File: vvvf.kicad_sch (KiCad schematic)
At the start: 106 parts, among them J1 Screw_Terminal_01x01, J2 Screw_Terminal_01x01, J3 Screw_Terminal_01x01, J4 Screw_Terminal_01x01, J5 Screw_Terminal_01x01, J6 Screw_Terminal_01x02, Q1 Q_NIGBT_GCE, Q2 Q_NIGBT_GCE, Q3 IPDD60R037CM8XTMA1, Q4 IPDD60R037CM8XTMA1, Q5 IPDD60R037CM8XTMA1, Q6 IPDD60R037CM8XTMA1, Q7 IPDD60R037CM8XTMA1, Q8 IPDD60R037CM8XTMA1, Q9 IPDD60R037CM8XTMA1, SW1 SW_Push, U1 TLP152, U2 TLP152, U3 UCC21520ADW, U4 TLP152, U5 ACS770xCB-200B-PFF, U6 UCC21520ADW, U7 UCC21520ADW, U8 ACS770xCB-200B-PFF

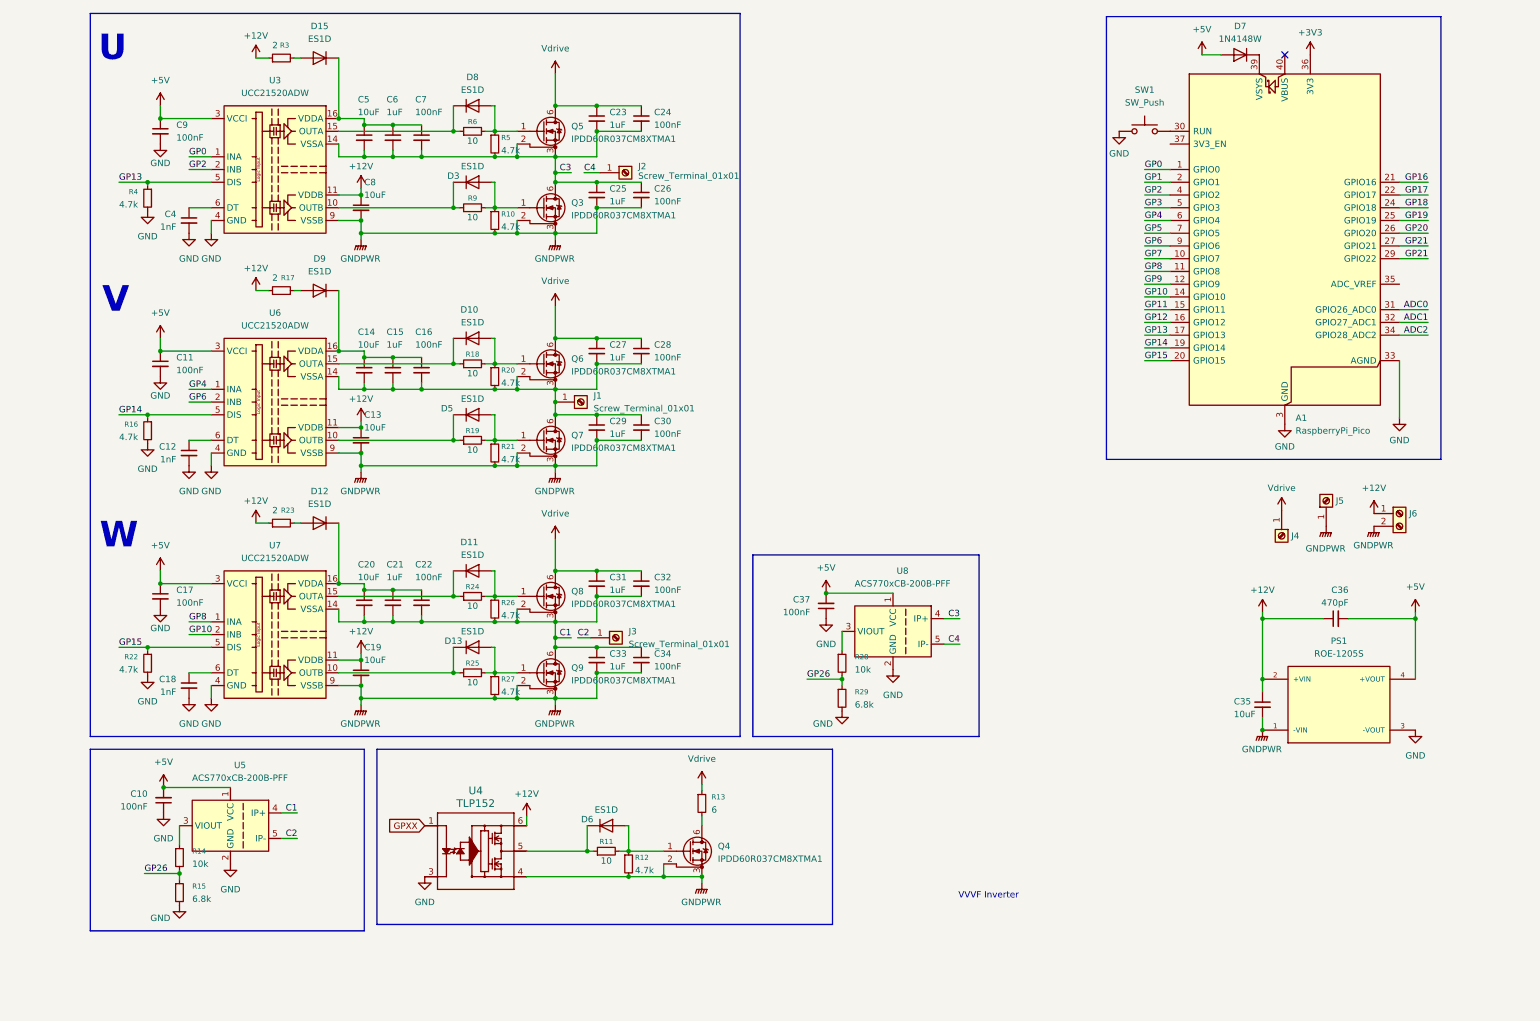
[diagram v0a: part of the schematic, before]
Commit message: Starting new routing with external IGBT
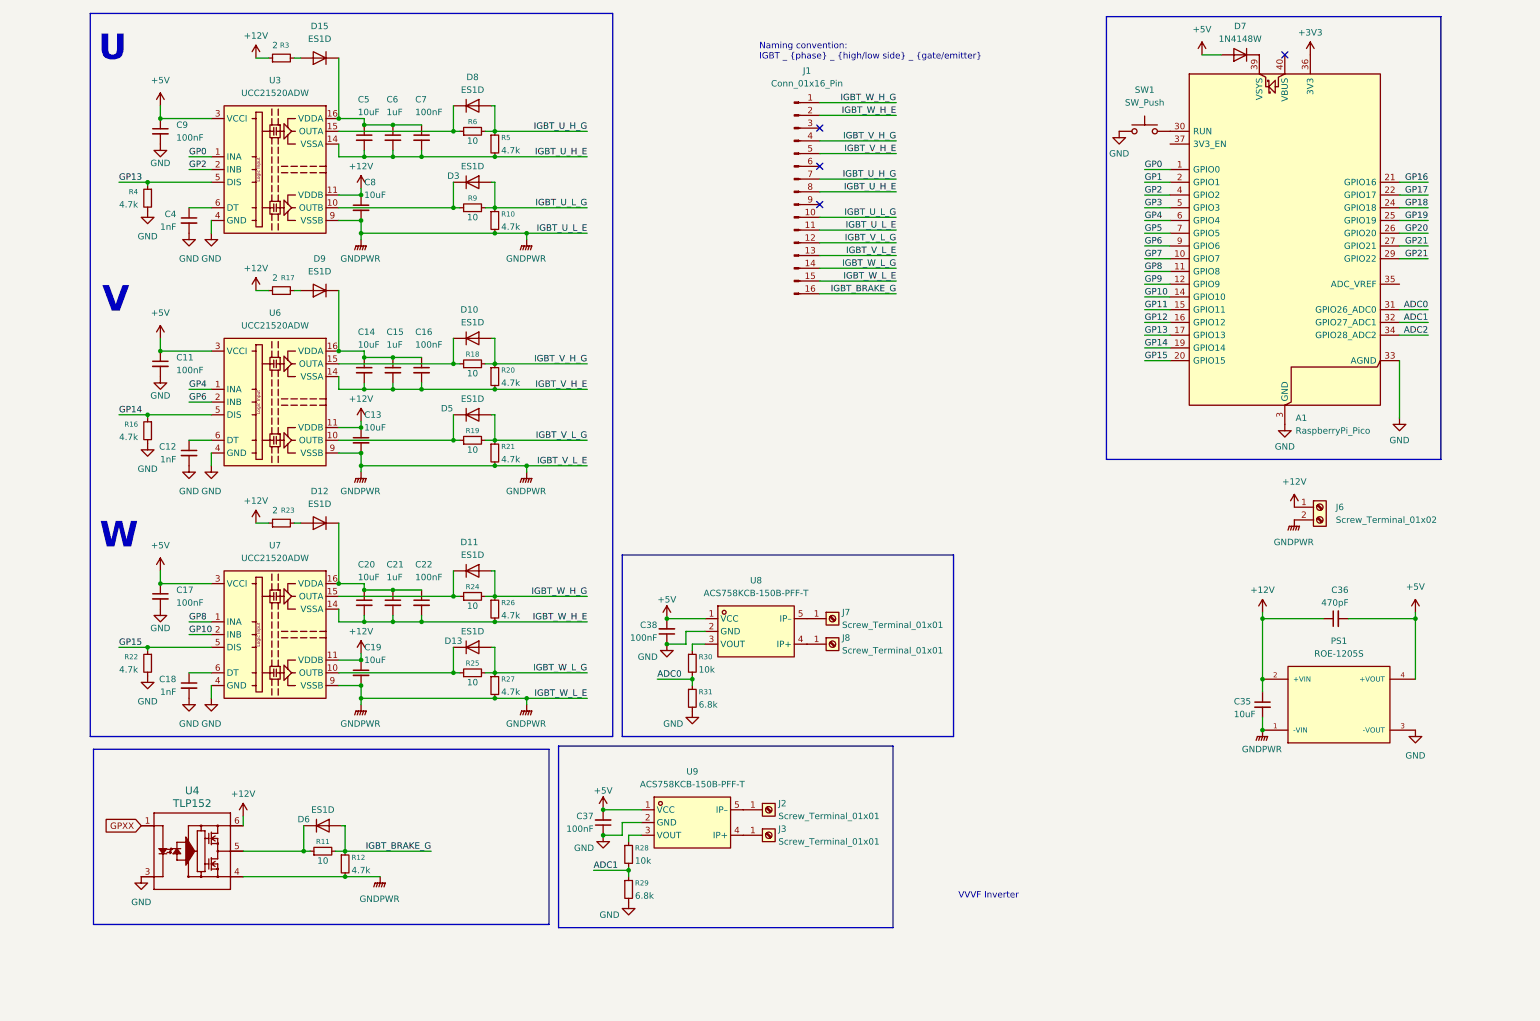
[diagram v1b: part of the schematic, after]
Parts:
- removed C10: 100nF, Capacitor_SMD:C_0603_1608Metric_Pad1.08x0.95mm_HandSolder, symbol Device:C_Small
- removed C23, C25, C27, C29, C31, C33: 1uF, Snapeda:B32923C3105M000_CAPRR2250W80L2650T1100H2050, symbol Device:C_Small
- removed C24, C26, C28, C30, C32, C34: 100nF, Snapeda:B32922C3104K289_CAPRR1500W80L1800T500H1050, symbol Device:C_Small
- removed J1, J4, J5: Screw_Terminal_01x01, symbol Connector:Screw_Terminal_01x01
- removed Q3, Q4, Q5, Q6, Q7, Q8, Q9: IPDD60R037CM8XTMA1, Package_TO_SOT_SMD:Infineon_PG-HDSOP-10-1, symbol Transistor_FET:IPDD60R050G7
- removed R13: 6, symbol Device:R_Small
- removed R14: 10k, Resistor_SMD:R_0603_1608Metric_Pad0.98x0.95mm_HandSolder, symbol Device:R_Small
- removed R15: 6.8k, symbol Device:R_Small
- removed U5, U8: ACS770xCB-200B-PFF, Sensor_Current:Allegro_CB_PFF, symbol Sensor_Current:ACS770xCB-200B-PFF
- added C38: 100nF, Capacitor_SMD:C_0603_1608Metric_Pad1.08x0.95mm_HandSolder, symbol Device:C_Small
- added J1: Conn_01x16_Pin, Connector_PinHeader_2.54mm:PinHeader_1x16_P2.54mm_Vertical, symbol Connector:Conn_01x16_Pin
- added J7, J8: Screw_Terminal_01x01, easyeda2kicad:CONN-TH_T44001, symbol Connector:Screw_Terminal_01x01
- added R30: 10k, Resistor_SMD:R_0603_1608Metric_Pad0.98x0.95mm_HandSolder, symbol Device:R_Small
- added R31: 6.8k, symbol Device:R_Small
- added U8, U9: ACS758KCB-150B-PFF-T, easyeda2kicad:SENSOR-TH_ACS758KCB-150B-PFF-T, symbol easyeda2kicad:ACS758KCB-150B-PFF-T_C6396159
- J2, J3: footprint (none) -> easyeda2kicad:CONN-TH_T44001
- J6: footprint (none) -> easyeda2kicad:CONN-TH_WJ126V-5.0-2P
- U3, U6, U7: LCSC Part (none) -> C2863027
- U4: footprint 5pin SO6_TOS -> Package_SO:SO-5-6_4.55x3.7mm_P1.27mm
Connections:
- net GP26 is gone; now on net ADC1: R28.2, R29.1
- net +5V: now also C38.2, U8.1 (VCC), U9.1 (VCC)
- net ADC0: now also R30.2, R31.1
- net GND: now also C38.1, R31.2, U8.2 (GND), U9.2 (GND)
- net GNDPWR: now also J1.11 (Pin_11), J1.13 (Pin_13), J1.15 (Pin_15)
- net IGBT_W_H_G: now reaches D11.2 (A), R24.2, R26.1
- net IGBT_W_H_G: now also J1.1 (Pin_1)
- net IGBT_V_H_G: now reaches D10.2 (A), R18.2, R20.1
- net IGBT_V_H_G: now also J1.4 (Pin_4)
- net at R28.1: now also U9.3 (VOUT)
- net IGBT_U_L_G: now reaches D3.2 (A), R10.1, R9.2
- net IGBT_U_L_G: now also J1.10 (Pin_10)
- net IGBT_V_H_E: now reaches C14.2, C15.2, C16.2, R20.2, U6.14 (VSSA)
- net IGBT_V_H_E: now also J1.5 (Pin_5)
- net IGBT_BRAKE_G: now reaches D6.2 (A), R11.2, R12.1
- net IGBT_BRAKE_G: now also J1.16 (Pin_16)
- net IGBT_U_H_G: now reaches D8.2 (A), R5.1, R6.2
- net IGBT_U_H_G: now also J1.7 (Pin_7)
- net IGBT_V_L_G: now reaches D5.2 (A), R19.2, R21.1
- net IGBT_V_L_G: now also J1.12 (Pin_12)
- net IGBT_W_L_G: now reaches D13.2 (A), R25.2, R27.1
- net IGBT_W_L_G: now also J1.14 (Pin_14)
- net C1 renamed IGBT_W_H_E
- net IGBT_W_H_E: now also J1.2 (Pin_2)
- net C2: no longer names the net of J3.1 (Pin_1)
- net C2: now also U9.4 (IP+)
- net C3 renamed IGBT_U_H_E
- net IGBT_U_H_E: now also J1.8 (Pin_8)
- net C4: no longer names the net of J2.1 (Pin_1)
- net C4: now also U9.5 (IP–)
- new net: J7.1 (Pin_1), U8.5 (IP–)
- new net: J8.1 (Pin_1), U8.4 (IP+)
- new net: R30.1, U8.3 (VOUT)
- no-connect marks 2 -> 5
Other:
- note added: "Naming convention: IGBT _ {phase} _ {high/low side} _ {gate/emitter}"
- moved on the sheet: C37, D6, R11, R12, R28, R29, U4

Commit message: sus commit
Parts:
- added C10: 100nF, Capacitor_SMD:C_0603_1608Metric_Pad1.08x0.95mm_HandSolder, symbol Device:C_Small
- added C23, C24: 22uF, symbol Device:C_Small
- added C25: 100nF, symbol Device:C_Small
- added J4, J5: Screw_Terminal_01x01, easyeda2kicad:CONN-TH_T44001, symbol Connector:Screw_Terminal_01x01
- added J9: Screw_Terminal_01x02, easyeda2kicad:CONN-TH_WJ126V-5.0-2P, symbol Connector:Screw_Terminal_01x02
- added R13: 10k, Resistor_SMD:R_0603_1608Metric_Pad0.98x0.95mm_HandSolder, symbol Device:R_Small
- added R14: 6.8k, Resistor_SMD:R_0603_1608Metric_Pad0.98x0.95mm_HandSolder, symbol Device:R_Small
- added R15, R33: 1M, Resistor_SMD:R_1206_3216Metric_Pad1.30x1.75mm_HandSolder, symbol Device:R_Small
- added R32: 1k, Resistor_SMD:R_1206_3216Metric_Pad1.30x1.75mm_HandSolder, symbol Device:R_Small
- added U11: LM7805_TO220, Package_TO_SOT_THT:TO-220-3_Vertical, symbol Regulator_Linear:LM7805_TO220
- added U12: AMC1303M2510DWVR, easyeda2kicad:SOIC-8_L7.5-W5.9-P1.27-LS11.5-BL-1, symbol easyeda2kicad:AMC1303M2510DWVR
- added U5: ACS758KCB-150B-PFF-T, easyeda2kicad:SENSOR-TH_ACS758KCB-150B-PFF-T, symbol easyeda2kicad:ACS758KCB-150B-PFF-T_C6396159
- R29, R31: footprint (none) -> Resistor_SMD:R_0603_1608Metric_Pad0.98x0.95mm_HandSolder
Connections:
- net +12V: now also C23.1, U11.1 (VI)
- net +3V3: now also C25.1, U12.8 (DVDD)
- net +5V: now also C10.2, U5.1 (VCC)
- net ADC0: now also R13.2, R14.1
- net GND: now also C10.1, C25.2, R14.2, U12.5 (DGND), U5.2 (GND)
- net GNDPWR: now also C23.2, C24.2, R32.2, U11.2 (GND), U12.3 (AINN), U12.4 (AGND)
- net Vdrive: now also J9.1 (Pin_1), R15.1
- new net: R15.2, R33.1
- new net: J5.1 (Pin_1), U5.4 (IP+)
- new net: R13.1, U5.3 (VOUT)
- new net: R32.1, R33.2, U12.2 (AINP)
- new net: J4.1 (Pin_1), U5.5 (IP–)
- new net +5V_UNISOLATED: C24.1, U11.3 (VO), U12.1 (AVDD)
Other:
- moved on the sheet: J1
